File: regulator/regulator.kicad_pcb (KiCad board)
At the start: 2 copper layers, 55.9 x 30.5 mm, 22 parts, among them J1 04x07, J1 Conn_01x02, J2 Conn_01x02, J4 Barrel_Jack_Switch, J5 Barrel_Jack_Switch, J6 Conn_01x02, J7 Conn_01x02, J8 Conn_01x02, J9 Conn_01x02

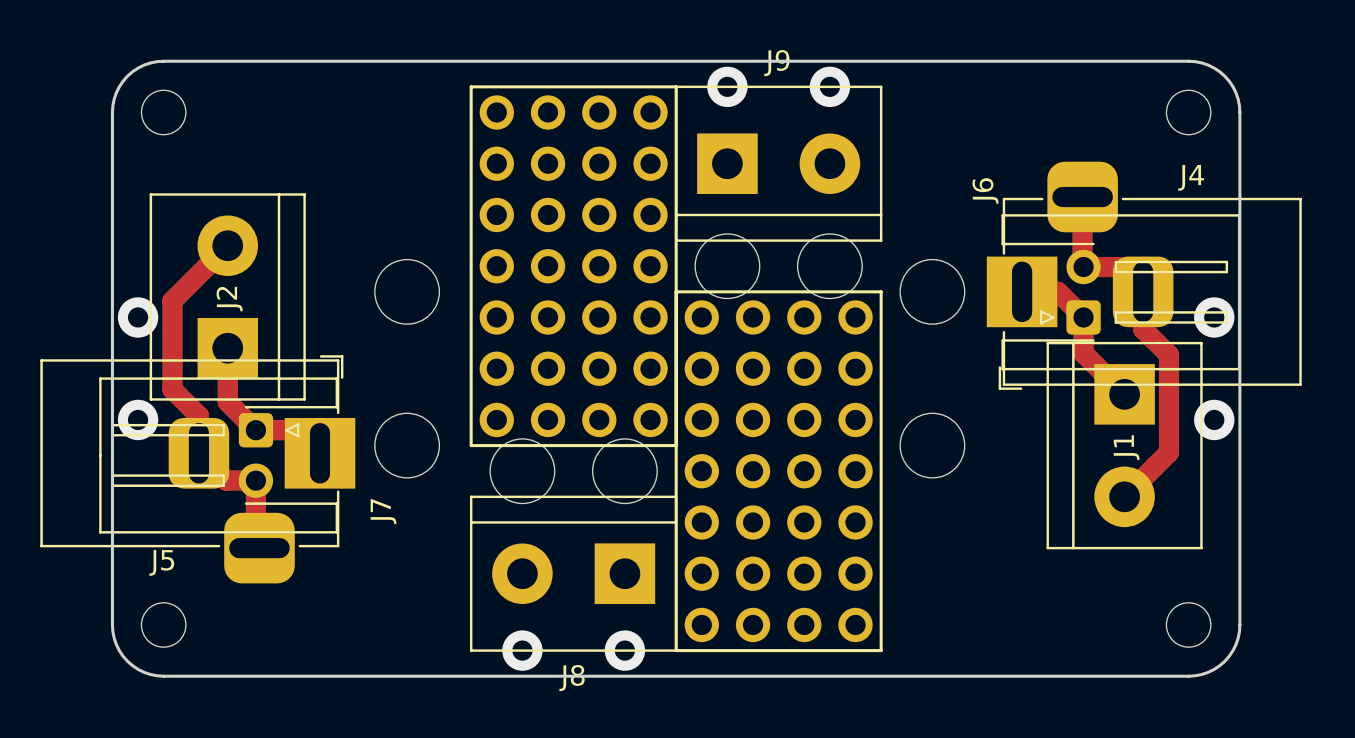
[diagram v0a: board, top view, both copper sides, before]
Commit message: prototype area enlarged
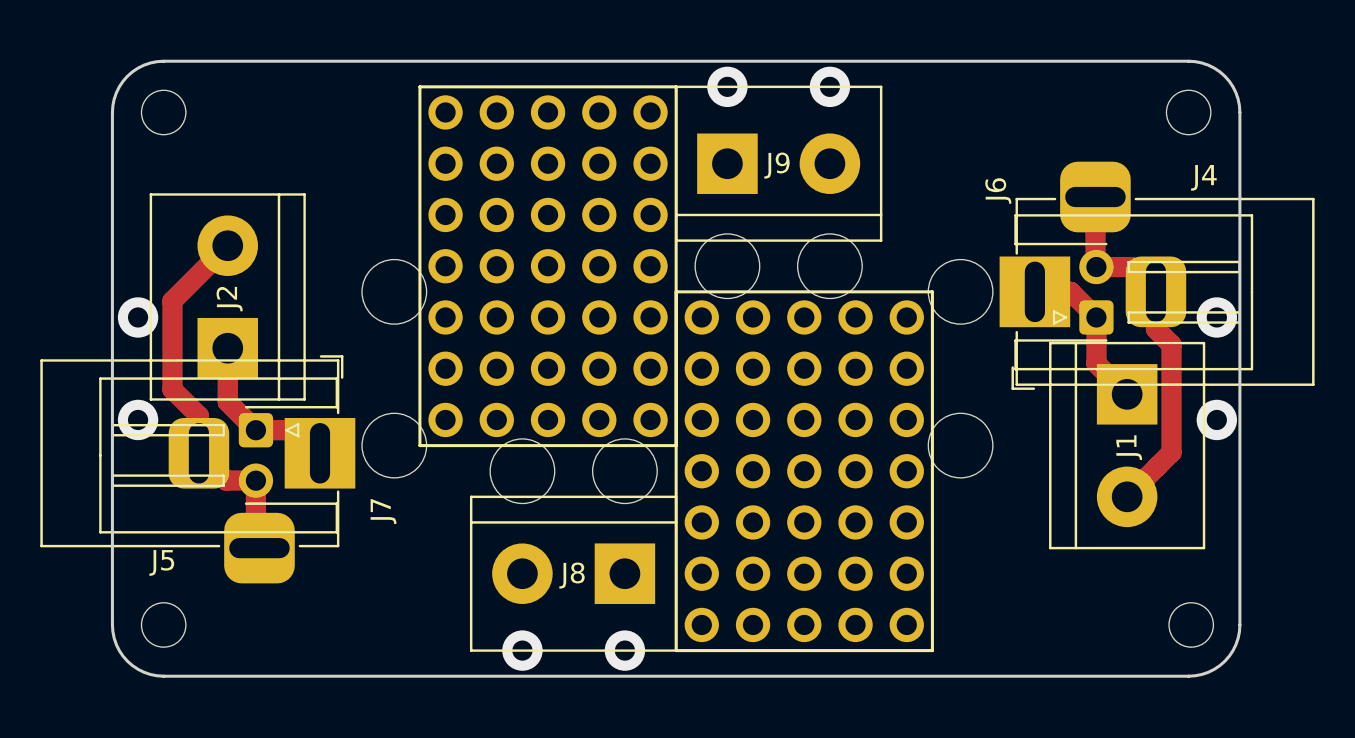
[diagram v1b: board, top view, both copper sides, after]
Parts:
- J1 (x2): footprint lib:Prototype_Area_2.54mm_04x07 -> lib:Prototype_Area_2.54mm_05x07
- moved J1 2.54 mm to (179.1, 97.8)
- moved REF** 1.40 mm to (181.7, 104.1)
- moved REF** 1.40 mm to (181.7, 96.5)
- moved REF** 0.64 mm to (153.7, 96.5)
- moved REF** 0.64 mm to (153.7, 104.1)
- moved J4 0.63 mm to (185.4, 96.5)
- moved J6 0.63 mm to (188.5, 97.8)
- moved REF** 0.13 mm to (193.2, 113.0)
- moved J1 0.13 mm to (190.0, 101.6)

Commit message: regulator update
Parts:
- removed the J1 at (179.1, 97.8)
- removed J9: Conn_01x02, TerminalBlock:TerminalBlock_bornier-2_P5.08mm
- removed the REF** at (175.3, 95.2)
- removed the REF** at (170.2, 95.2)
- added J1: 02x03, lib:Prototype_Area_2.54mm_02x03, F.Cu at (179.1, 88.9)
- added J1: 04x07, lib:Prototype_Area_2.54mm_04x10, F.Cu at (176.5, 88.9)
- added J1: 03x03, lib:Prototype_Area_2.54mm_03x03, F.Cu at (184.2, 106.7)
- added J1: 03x03, lib:Prototype_Area_2.54mm_03x03, F.Cu at (156.2, 88.9)
- added J1: 02x03, lib:Prototype_Area_2.54mm_02x03, F.Cu at (151.1, 109.2)
- J1: footprint lib:Prototype_Area_2.54mm_05x07 -> lib:Prototype_Area_2.54mm_04x06
- moved REF** 1.80 mm to (154.9, 97.8)
- moved REF** 1.80 mm to (154.9, 102.9)
- moved REF** 1.80 mm to (191.9, 111.8)
- moved REF** 1.80 mm to (180.5, 97.8)
- moved REF** 1.80 mm to (191.8, 88.9)
- moved REF** 1.80 mm to (143.5, 88.9)
- moved REF** 1.80 mm to (180.5, 102.9)
- moved REF** 1.80 mm to (143.5, 111.8)
- moved J1 1.27 mm to (166.4, 88.9)
- moved J2 1.27 mm to (146.7, 99.3)
- moved J5 1.27 mm to (151.3, 104.5)
- moved J1 1.27 mm to (188.7, 101.6)
- moved J4 1.27 mm to (184.2, 96.5)
- moved J6 1.27 mm to (187.2, 97.8)
- moved J7 1.27 mm to (148.1, 103.4)
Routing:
- net (no net): vias 8 -> 4
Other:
- board size 55.9 x 30.5 mm -> 53.3 x 27.9 mm

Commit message: regulator update
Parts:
- removed the J1 at (179.1, 88.9)
- removed the J1 at (166.4, 88.9)
- removed the J1 at (176.5, 88.9)
- removed the J1 at (188.7, 101.6)
- removed the J1 at (184.2, 106.7)
- removed the J1 at (156.2, 88.9)
- removed the J1 at (151.1, 109.2)
- removed J4, J5: Barrel_Jack_Switch, Connector_BarrelJack:BarrelJack_Horizontal
- removed J6, J7: Conn_01x02, Connector_JST:JST_XH_S02B-XH-A-1_1x02_P2.50mm_Horizontal
- removed J8: Conn_01x02, TerminalBlock:TerminalBlock_bornier-2_P5.08mm
- removed the REF** at (160.0, 105.4)
- removed the REF** at (154.9, 97.8)
- removed the REF** at (165.1, 105.4)
- removed the REF** at (180.5, 102.9)
- removed the REF** at (180.5, 97.8)
- removed the REF** at (154.9, 102.9)
- removed the REF** at (191.8, 88.9)
- removed the REF** at (191.9, 111.8)
- removed the REF** at (143.5, 88.9)
- removed the REF** at (143.5, 111.8)
- added J1: Conn_01x02, TerminalBlock:TerminalBlock_bornier-2_P5.08mm, F.Cu at (186.7, 105.4)
- added J1: 0x04, lib:Prototype_Area_2.54mm_01x04, F.Cu at (156.2, 94.0)
- added J10: 09x10, lib:Prototype_Area_2.54mm_08x08, F.Cu at (176.5, 88.9)
- added REF**: MountingHole_2.5mm, MountingHole:MountingHole_2.5mm, F.Cu at (154.9, 106.7)
- added REF**: MountingHole_2.5mm, MountingHole:MountingHole_2.5mm, F.Cu at (154.9, 88.9)
- added REF**: MountingHole_2.5mm, MountingHole:MountingHole_2.5mm, F.Cu at (191.8, 106.7)
- added REF**: MountingHole_2.5mm, MountingHole:MountingHole_2.5mm, F.Cu at (191.8, 88.9)
- added SW1: SW_SPDT, Connector_PinHeader_2.54mm:PinHeader_1x03_P2.54mm_Vertical, F.Cu at (186.1, 88.3)
- J2: value Conn_01x02 -> Barrel_Jack_Switch; footprint TerminalBlock:TerminalBlock_bornier-2_P5.08mm -> Connector_BarrelJack:BarrelJack_Horizontal
- moved J2 33.8 mm to (180.3, 96.5), turned to 180 degrees
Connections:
- J2 pad 2: Net-(J2-Pad2) -> GND
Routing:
- net Net-(J2-Pad2): track 18.8 -> 0.00 mm
- net Net-(J1-Pad2): track 18.3 -> 0.00 mm
- net Net-(J1-Pad1): track 8.02 -> 0.00 mm
- net Net-(J2-Pad1): track 8.29 -> 9.82 mm
- net (no net): vias 4 -> 0
- added copper zone on F.Cu, net GND
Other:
- board size 53.3 x 27.9 mm -> 41.9 x 22.9 mm
- net class Default: trace_width 1 -> 0.75
- board text added: "+"
- board text added: "OFF"
- board text added: "ON"
- board text added: "■3.3V ■5V ■12V"

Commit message: add/enlarge holes
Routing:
- net GND: vias 0 -> 2
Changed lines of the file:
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@@
     (thickness 1.6)
     (drawings 14)
-    (tracks 5)
+    (tracks 7)
     (zones 0)
     (modules 9)
@@
   (gr_line (start 194.31 88.9) (end 194.31 106.68) (layer Edge.Cuts) (width 0.15))
   (gr_line (start 154.94 86.36) (end 191.77 86.36) (layer Edge.Cuts) (width 0.15))
+  (via (at 181.61 108.204) (size 1.1) (drill 1) (layers F.Cu B.Cu) (net 2))
+  (via (at 186.69 108.204) (size 1.1) (drill 1) (layers F.Cu B.Cu) (net 2))
   (segment (start 180.34 94.02) (end 180.34 96.52) (width 0.75) (layer B.Cu) (net 3))
   (segment (start 180.34 91.009002) (end 180.34 94.02) (width 0.75) (layer B.Cu) (net 3))
@@
     (polygon
       (pts
-        (xy 177.8 87.63) (xy 187.96 87.63) (xy 191.77 91.44) (xy 191.77 104.14) (xy 187.96 107.95)
-        (xy 177.8 107.95)
+        (xy 177.8 86.36) (xy 186.69 86.36) (xy 191.77 91.44) (xy 191.77 104.14) (xy 186.69 109.22)
+        (xy 177.8 109.22)
       )
     )
